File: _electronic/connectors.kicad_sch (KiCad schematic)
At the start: 7 parts

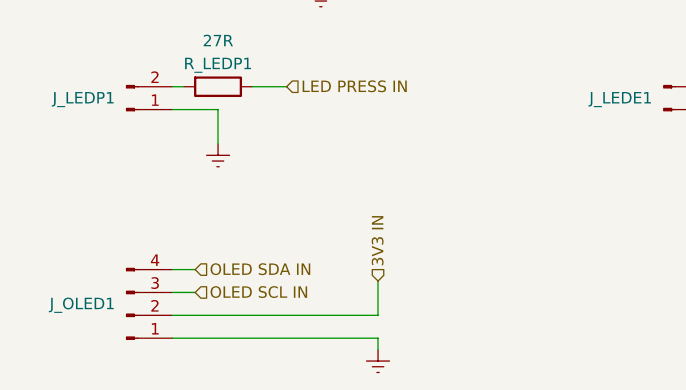
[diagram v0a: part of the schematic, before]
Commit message: revised pcb: direct power, leds, ftdi w/o 3v3
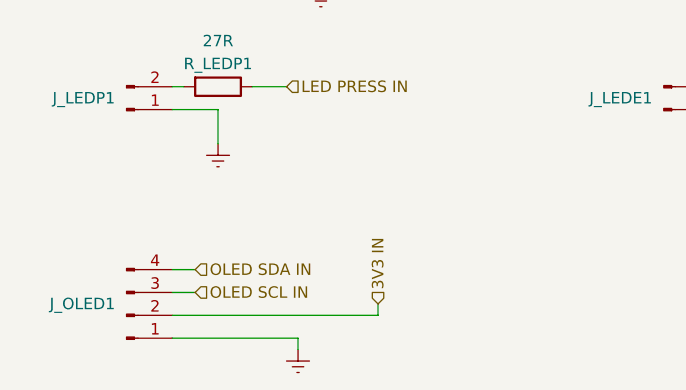
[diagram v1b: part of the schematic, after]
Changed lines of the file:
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@@
     (company "Andrei Speridiao")
   )
-  (wire (pts (xy 138.43 129.54) (xy 138.43 125.73))
+  (wire (pts (xy 138.43 128.27) (xy 138.43 129.54))
     (stroke (width 0) (type default) (color 0 0 0 0))
   )
@@
     (stroke (width 0) (type default) (color 0 0 0 0))
   )
+  (wire (pts (xy 115.57 129.54) (xy 138.43 129.54))
+    (stroke (width 0) (type default) (color 0 0 0 0))
+  )
   (wire (pts (xy 191.77 88.9) (xy 191.77 92.71))
     (stroke (width 0) (type default) (color 0 0 0 0))
@@
     (stroke (width 0) (type default) (color 0 0 0 0))
   )
-  (wire (pts (xy 115.57 132.08) (xy 138.43 132.08))
-    (stroke (width 0) (type default) (color 0 0 0 0))
-  )
-  (wire (pts (xy 138.43 132.08) (xy 138.43 133.35))
+  (wire (pts (xy 129.54 132.08) (xy 129.54 133.35))
     (stroke (width 0) (type default) (color 0 0 0 0))
   )
@@
     (stroke (width 0) (type default) (color 0 0 0 0))
   )
+  (wire (pts (xy 115.57 132.08) (xy 129.54 132.08))
+    (stroke (width 0) (type default) (color 0 0 0 0))
+  )
   (wire (pts (xy 115.57 106.68) (xy 120.65 106.68))
     (stroke (width 0) (type default) (color 0 0 0 0))
@@
   )
   (wire (pts (xy 177.8 83.82) (xy 175.26 83.82))
-    (stroke (width 0) (type default) (color 0 0 0 0))
-  )
-  (wire (pts (xy 115.57 129.54) (xy 138.43 129.54))
     (stroke (width 0) (type default) (color 0 0 0 0))
   )
@@
     (effects (font (size 1.27 1.27)) (justify left))
   )
-  (hierarchical_label "3V3 IN" (shape input) (at 138.43 125.73 90)
+  (hierarchical_label "3V3 IN" (shape input) (at 138.43 128.27 90)
     (effects (font (size 1.27 1.27)) (justify left))
   )
@@
     (pin "1")
   )
-  (symbol (lib_id "power:GNDREF") (at 138.43 133.35 0) (unit 1)
-    (in_bom yes) (on_board yes) (fields_autoplaced)
-    (property "Reference" "#PWR0141" (id 0) (at 138.43 139.7 0)
-      (effects (font (size 1.27 1.27)) hide)
-    )
-    (property "Value" "GNDREF" (id 1) (at 138.43 138.43 0)
-      (effects (font (size 1.27 1.27)) hide)
-    )
-    (property "Footprint" "" (id 2) (at 138.43 133.35 0)
-      (effects (font (size 1.27 1.27)) hide)
-    )
-    (property "Datasheet" "" (id 3) (at 138.43 133.35 0)
-      (effects (font (size 1.27 1.27)) hide)
-    )
+  (symbol (lib_id "power:GNDREF") (at 129.54 133.35 0) (unit 1)
+    (in_bom yes) (on_board yes) (fields_autoplaced)
+    (property "Reference" "#PWR0141" (id 0) (at 129.54 139.7 0)
+      (effects (font (size 1.27 1.27)) hide)
+    )
+    (property "Value" "GNDREF" (id 1) (at 129.54 138.43 0)
+      (effects (font (size 1.27 1.27)) hide)
+    )
+    (property "Footprint" "" (id 2) (at 129.54 133.35 0)
+      (effects (font (size 1.27 1.27)) hide)
+    )
+    (property "Datasheet" "" (id 3) (at 129.54 133.35 0)
+      (effects (font (size 1.27 1.27)) hide)
+    )

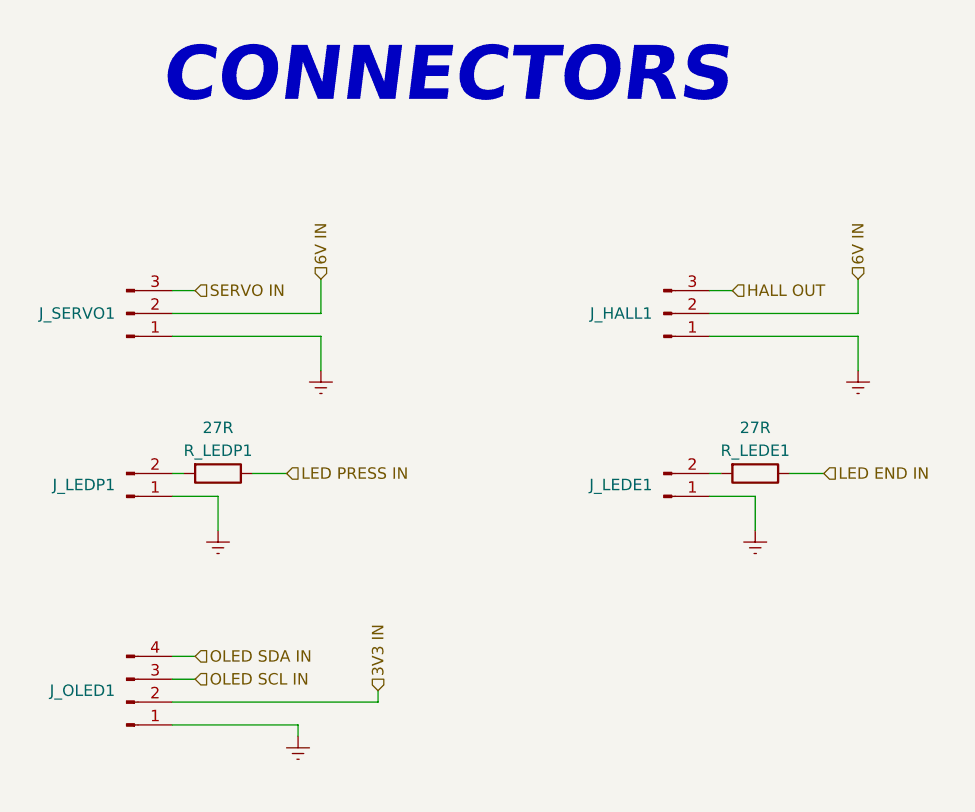
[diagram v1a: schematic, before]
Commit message: led resistor revision, b.o.m. and pcb anotation
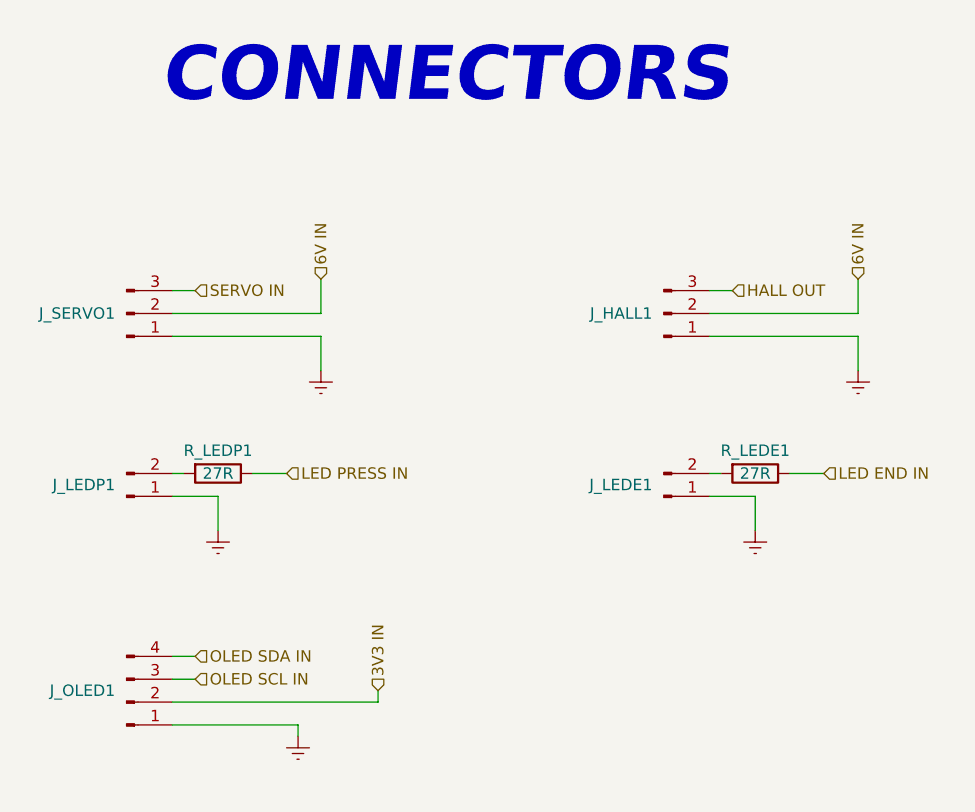
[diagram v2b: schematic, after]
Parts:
- R_LEDE1, R_LEDP1: # CMP0603-FX-27R0ELF -> ERJ-3EKF27R0V
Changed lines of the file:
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@@
     (in_bom yes) (on_board yes)
     (property "Reference" "R_LEDP1" (id 0) (at 120.65 101.6 90))
-    (property "Value" "27R" (id 1) (at 120.65 99.06 90))
+    (property "Value" "27R" (id 1) (at 120.65 104.14 90))
     (property "Footprint" "Resistor_SMD:R_0603_1608Metric_Pad0.98x0.95mm_HandSolder" (id 2) (at 120.65 102.362 90)
       (effects (font (size 1.27 1.27)) hide)
@@
       (effects (font (size 1.27 1.27)) hide)
     )
-    (property "#" "CMP0603-FX-27R0ELF" (id 4) (at 119.38 106.68 0)
+    (property "#" "ERJ-3EKF27R0V" (id 4) (at 119.38 106.68 0)
       (effects (font (size 1.27 1.27) italic) (justify left) hide)
     )
@@
     (in_bom yes) (on_board yes)
     (property "Reference" "R_LEDE1" (id 0) (at 180.34 101.6 90))
-    (property "Value" "27R" (id 1) (at 180.34 99.06 90))
+    (property "Value" "27R" (id 1) (at 180.34 104.14 90))
     (property "Footprint" "Resistor_SMD:R_0603_1608Metric_Pad0.98x0.95mm_HandSolder" (id 2) (at 180.34 102.362 90)
       (effects (font (size 1.27 1.27)) hide)
@@
       (effects (font (size 1.27 1.27)) hide)
     )
-    (property "#" "CMP0603-FX-27R0ELF" (id 4) (at 179.07 106.68 0)
+    (property "#" "ERJ-3EKF27R0V" (id 4) (at 179.07 106.68 0)
       (effects (font (size 1.27 1.27) italic) (justify left) hide)
     )

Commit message: schematics and pcb cleanup
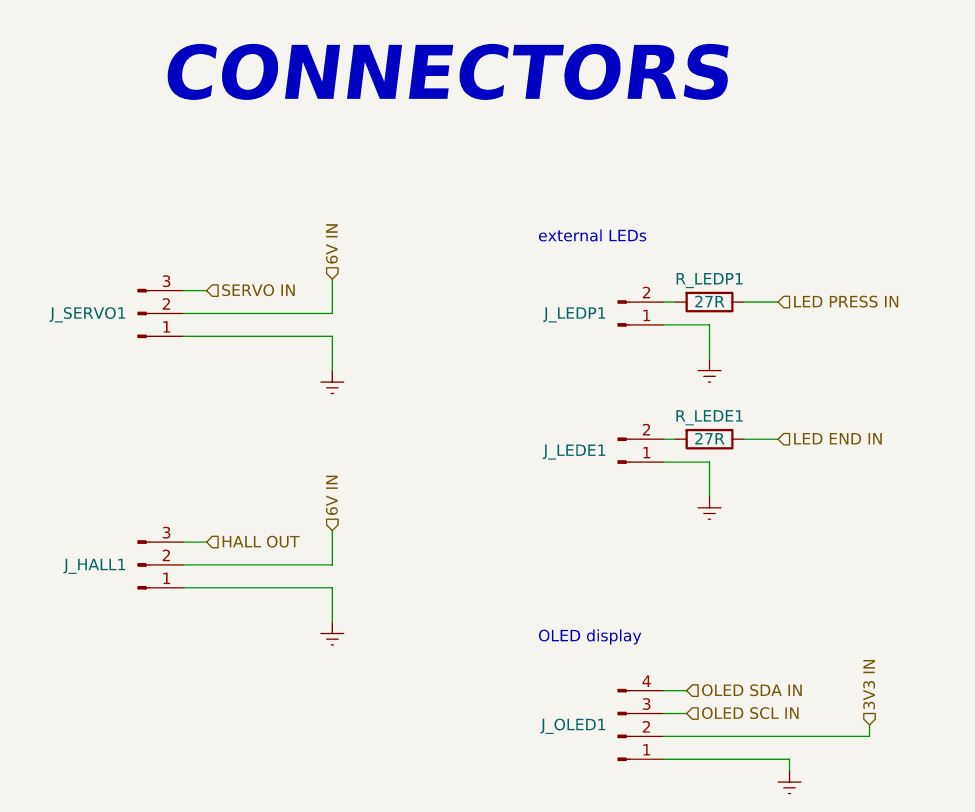
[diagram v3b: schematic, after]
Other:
- note added: "OLED display"
- note added: "external LEDs"
- title: E-TKT -> E-TKT v1.0
- moved on the sheet: J_HALL1, J_LEDE1, J_LEDP1, J_OLED1, J_SERVO1, R_LEDE1, R_LEDP1

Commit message: fixed hall header on pcb
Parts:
- J_HALL1: footprint Connector_PinSocket_2.54mm:PinSocket_1x03_P2.54mm_Vertical -> Connector_PinHeader_2.54mm:PinHeader_1x03_P2.54mm_Vertical
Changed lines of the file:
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@@
       (effects (font (size 1.27 1.27)) (justify right) hide)
     )
-    (property "Footprint" "Connector_PinSocket_2.54mm:PinSocket_1x03_P2.54mm_Vertical" (id 2) (at 111.76 114.3 0)
+    (property "Footprint" "Connector_PinHeader_2.54mm:PinHeader_1x03_P2.54mm_Vertical" (id 2) (at 111.76 114.3 0)
       (effects (font (size 1.27 1.27)) hide)
     )
